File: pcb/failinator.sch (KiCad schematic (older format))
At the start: 18 parts, among them P1 CONN_01X04, P2 CONN_01X10, P3 CONN_01X10, P4 CONN_01X06, U1 MAX7219, U2 RASPIPLUSHEADER

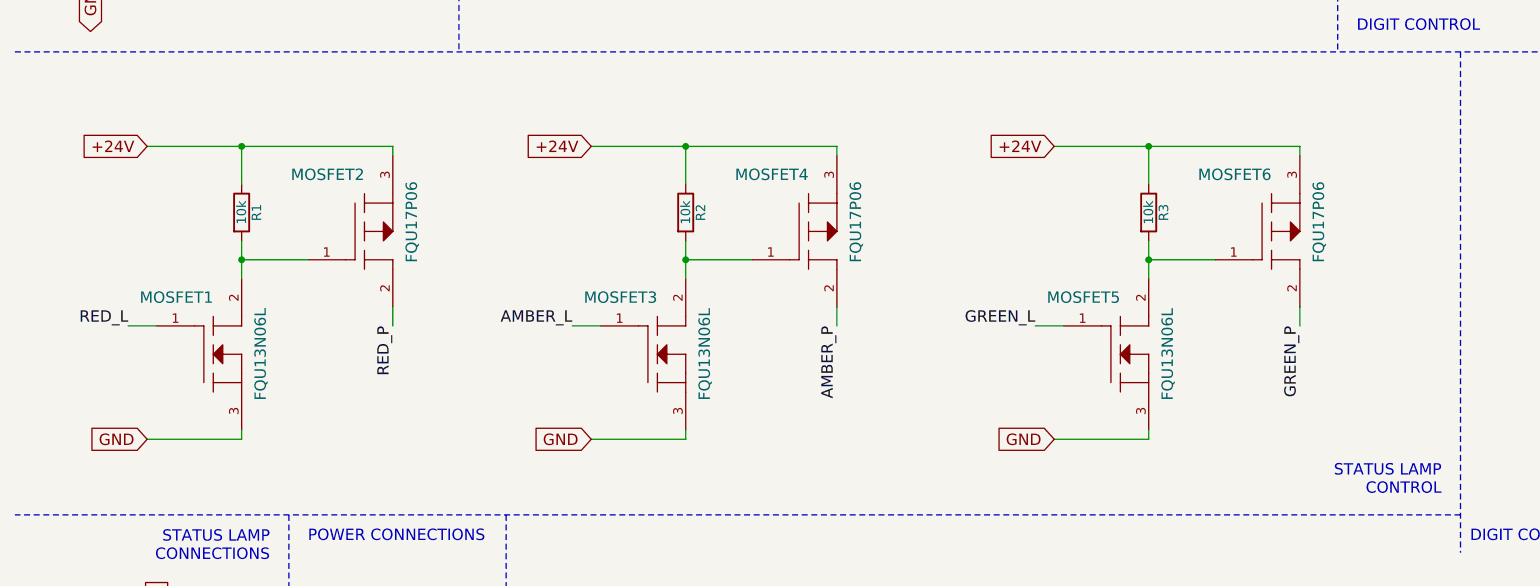
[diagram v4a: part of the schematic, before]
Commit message: Factor out the MOSFET switches into a separate sheet.
There will be a lot more of these soon once we start using a similar
pattern to switch the LED segments.
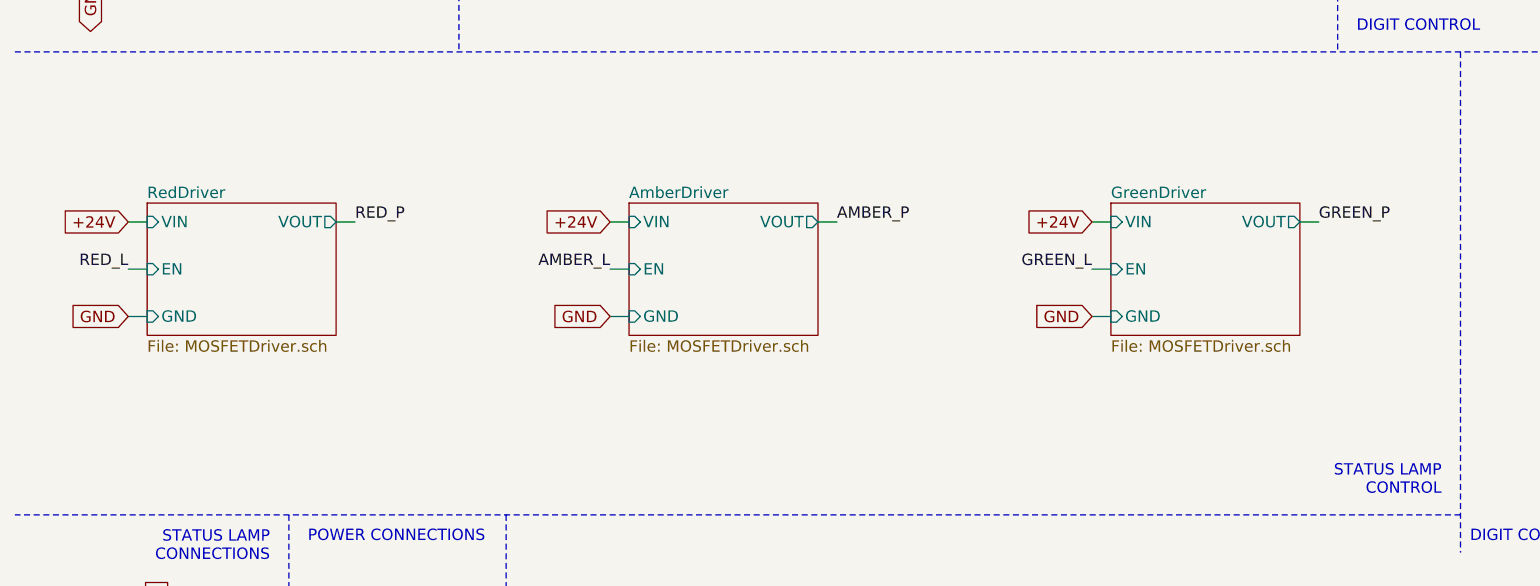
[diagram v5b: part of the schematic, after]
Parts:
- removed MOSFET1, MOSFET3, MOSFET5: FQU13N06L, failinator:TO-251AA, symbol FQU13N06L
- removed MOSFET2, MOSFET4, MOSFET6: FQU17P06, failinator:TO-251AA, symbol FQU17P06
- removed R1, R2, R3: 10k, Discret:R3, symbol R
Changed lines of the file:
@@
 $Descr USLetter 11000 8500
 encoding utf-8
-Sheet 1 1
+Sheet 1 4
 Title "Failinator"
 Date ""
@@
 Wire Wire Line
 	1350 7550 1400 7550
-$Comp
-L FQU13N06L MOSFET1
-U 1 1 5604F114
-P 1500 5700
-F 0 "MOSFET1" H 1650 6000 60  0000 R CNN
-F 1 "FQU13N06L" V 1900 5700 60  0000 C CNN
-F 2 "failinator:TO-251AA" H 1500 5700 60  0001 C CNN
-F 3 "" H 1500 5700 60  0000 C CNN
-	1    1500 5700
-	1    0    0    -1
-$EndComp
-Text GLabel 1300 6150 0    60   Input ~ 0
-GND
-Text GLabel 1300 4600 0    60   Input ~ 0
+Text GLabel 1200 5500 0    60   Input ~ 0
+GND
+Text GLabel 1200 5000 0    60   Input ~ 0
 +24V
-$Comp
-L R R1
-U 1 1 5604FF36
-P 1800 4950
-F 0 "R1" V 1880 4950 50  0000 C CNN
-F 1 "10k" V 1800 4950 50  0000 C CNN
-F 2 "Discret:R3" V 1730 4950 30  0001 C CNN
-F 3 "" H 1800 4950 30  0000 C CNN
-	1    1800 4950
-	1    0    0    -1
-$EndComp
-$Comp
-L FQU17P06 MOSFET2
-U 1 1 56050258
-P 2300 5050
-F 0 "MOSFET2" H 2450 5350 60  0000 R CNN
-F 1 "FQU17P06" V 2700 5100 60  0000 C CNN
-F 2 "failinator:TO-251AA" H 2300 5050 60  0001 C CNN
-F 3 "" H 2300 5050 60  0000 C CNN
-	1    2300 5050
-	1    0    0    -1
-$EndComp
-Text Label 1200 5550 2    60   ~ 0
+Text Label 1200 5250 2    60   ~ 0
 RED_L
-Text Label 2600 5550 3    60   ~ 0
+Text Label 2400 5000 0    60   ~ 0
 RED_P
-Wire Wire Line
-	1800 4800 1800 4600
-Wire Wire Line
-	1800 5100 1800 5300
-Wire Wire Line
-	1200 5550 1350 5550
-Wire Wire Line
-	1300 6150 1800 6150
-Wire Wire Line
-	1800 6150 1800 6100
-Wire Wire Line
-	1300 4600 2600 4600
-Wire Wire Line
-	2600 4600 2600 4650
-Connection ~ 1800 4600
-Wire Wire Line
-	2600 5450 2600 5550
-Wire Wire Line
-	2150 5200 1800 5200
-Connection ~ 1800 5200
-$Comp
-L FQU13N06L MOSFET3
-U 1 1 56051AD8
-P 3850 5700
-F 0 "MOSFET3" H 4000 6000 60  0000 R CNN
-F 1 "FQU13N06L" V 4250 5700 60  0000 C CNN
-F 2 "failinator:TO-251AA" H 3850 5700 60  0001 C CNN
-F 3 "" H 3850 5700 60  0000 C CNN
-	1    3850 5700
-	1    0    0    -1
-$EndComp
-Text GLabel 3650 6150 0    60   Input ~ 0
-GND
-Text GLabel 3650 4600 0    60   Input ~ 0
+Text GLabel 3750 5500 0    60   Input ~ 0
+GND
+Text GLabel 3750 5000 0    60   Input ~ 0
 +24V
-$Comp
-L R R2
-U 1 1 56051AE0
-P 4150 4950
-F 0 "R2" V 4230 4950 50  0000 C CNN
-F 1 "10k" V 4150 4950 50  0000 C CNN
-F 2 "Discret:R3" V 4080 4950 30  0001 C CNN
-F 3 "" H 4150 4950 30  0000 C CNN
-	1    4150 4950
-	1    0    0    -1
-$EndComp
-$Comp
-L FQU17P06 MOSFET4
-U 1 1 56051AE6
-P 4650 5050
-F 0 "MOSFET4" H 4800 5350 60  0000 R CNN
-F 1 "FQU17P06" V 5050 5100 60  0000 C CNN
-F 2 "failinator:TO-251AA" H 4650 5050 60  0001 C CNN
-F 3 "" H 4650 5050 60  0000 C CNN
-	1    4650 5050
-	1    0    0    -1
-$EndComp
-Text Label 3550 5550 2    60   ~ 0
+Text Label 3750 5250 2    60   ~ 0
 AMBER_L
-Text Label 4950 5550 3    60   ~ 0
+Text Label 4950 5000 0    60   ~ 0
 AMBER_P
-Wire Wire Line
-	4150 4800 4150 4600
-Wire Wire Line
-	4150 5100 4150 5300
-Wire Wire Line
-	3550 5550 3700 5550
-Wire Wire Line
-	3650 6150 4150 6150
-Wire Wire Line
-	4150 6150 4150 6100
-Wire Wire Line
-	3650 4600 4950 4600
-Wire Wire Line
-	4950 4600 4950 4650
-Connection ~ 4150 4600
-Wire Wire Line
-	4950 5450 4950 5550
-Wire Wire Line
-	4500 5200 4150 5200
-Connection ~ 4150 5200
-$Comp
-L FQU13N06L MOSFET5
-U 1 1 56051BEF
-P 6300 5700
-F 0 "MOSFET5" H 6450 6000 60  0000 R CNN
-F 1 "FQU13N06L" V 6700 5700 60  0000 C CNN
-F 2 "failinator:TO-251AA" H 6300 5700 60  0001 C CNN
-F 3 "" H 6300 5700 60  0000 C CNN
-	1    6300 5700
-	1    0    0    -1
-$EndComp
-Text GLabel 6100 6150 0    60   Input ~ 0
-GND
-Text GLabel 6100 4600 0    60   Input ~ 0
+Text GLabel 6300 5500 0    60   Input ~ 0
+GND
+Text GLabel 6300 5000 0    60   Input ~ 0
 +24V
-$Comp
-L R R3
-U 1 1 56051BF7
-P 6600 4950
-F 0 "R3" V 6680 4950 50  0000 C CNN
-F 1 "10k" V 6600 4950 50  0000 C CNN
-F 2 "Discret:R3" V 6530 4950 30  0001 C CNN
-F 3 "" H 6600 4950 30  0000 C CNN
-	1    6600 4950
-	1    0    0    -1
-$EndComp
-$Comp
-L FQU17P06 MOSFET6
-U 1 1 56051BFD
-P 7100 5050
-F 0 "MOSFET6" H 7250 5350 60  0000 R CNN
-F 1 "FQU17P06" V 7500 5100 60  0000 C CNN
-F 2 "failinator:TO-251AA" H 7100 5050 60  0001 C CNN
-F 3 "" H 7100 5050 60  0000 C CNN
-	1    7100 5050
-	1    0    0    -1
-$EndComp
-Text Label 6000 5550 2    60   ~ 0
+Text Label 6300 5250 2    60   ~ 0
 GREEN_L
-Text Label 7400 5550 3    60   ~ 0
+Text Label 7500 5000 0    60   ~ 0
 GREEN_P
-Wire Wire Line
-	6600 4800 6600 4600
-Wire Wire Line
-	6600 5100 6600 5300
-Wire Wire Line
-	6000 5550 6150 5550
-Wire Wire Line
-	6100 6150 6600 6150
-Wire Wire Line
-	6600 6150 6600 6100
-Wire Wire Line
-	6100 4600 7400 4600
-Wire Wire Line
-	7400 4600 7400 4650
-Connection ~ 6600 4600
-Wire Wire Line
-	7400 5450 7400 5550
-Wire Wire Line
-	6950 5200 6600 5200
-Connection ~ 6600 5200
 Wire Notes Line
 	2950 600  2950 4100
@@
 Text Label 9250 5950 2    60   ~ 0
 DIG1
+$Sheet
+S 1300 4900 1000 700
+U 568778A1
+F0 "RedDriver" 60
+F1 "MOSFETDriver.sch" 60
+F2 "VIN" I L 1300 5000 60
+F3 "GND" I L 1300 5500 60
+F4 "EN" I L 1300 5250 60
+F5 "VOUT" O R 2300 5000 60
+$EndSheet
+Wire Wire Line
+	2300 5000 2400 5000
+Wire Wire Line
+	1200 5000 1300 5000
+Wire Wire Line
+	1200 5250 1300 5250
+Wire Wire Line
+	1200 5500 1300 5500
+$Sheet
+S 3850 4900 1000 700
+U 56879543
+F0 "AmberDriver" 60
+F1 "MOSFETDriver.sch" 60
+F2 "VIN" I L 3850 5000 60
+F3 "GND" I L 3850 5500 60
+F4 "EN" I L 3850 5250 60
+F5 "VOUT" O R 4850 5000 60
+$EndSheet
+$Sheet
+S 6400 4900 1000 700
+U 5687AB7C
+F0 "GreenDriver" 60
+F1 "MOSFETDriver.sch" 60
+F2 "VIN" I L 6400 5000 60
+F3 "GND" I L 6400 5500 60
+F4 "EN" I L 6400 5250 60
+F5 "VOUT" O R 7400 5000 60
+$EndSheet
+Wire Wire Line
+	3750 5000 3850 5000
+Wire Wire Line
+	3750 5250 3850 5250
+Wire Wire Line
+	3750 5500 3850 5500
+Wire Wire Line
+	4850 5000 4950 5000
+Wire Wire Line
+	6300 5000 6400 5000
+Wire Wire Line
+	6300 5250 6400 5250
+Wire Wire Line
+	6300 5500 6400 5500
+Wire Wire Line
+	7400 5000 7500 5000
 $EndSCHEMATC

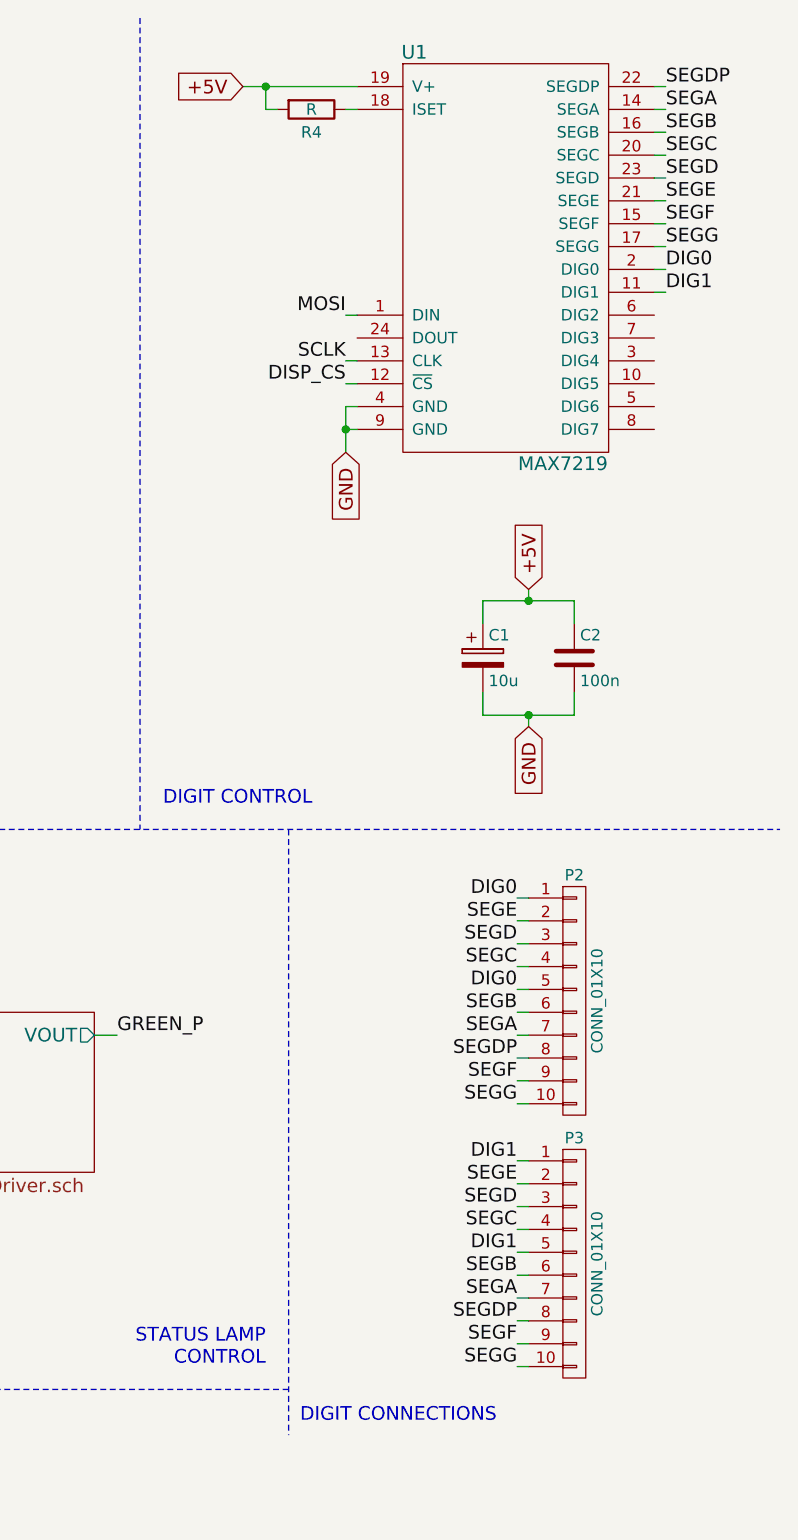
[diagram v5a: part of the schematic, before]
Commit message: Remove the MAX7219-based digit driver sub-circuit
The digit driver on v0.1 was not correct, providing only 5V to LED
segments that have a forward voltage of more like 27V, causing them to
not show at all.

A replacement for this will be added in a subsequent commit.
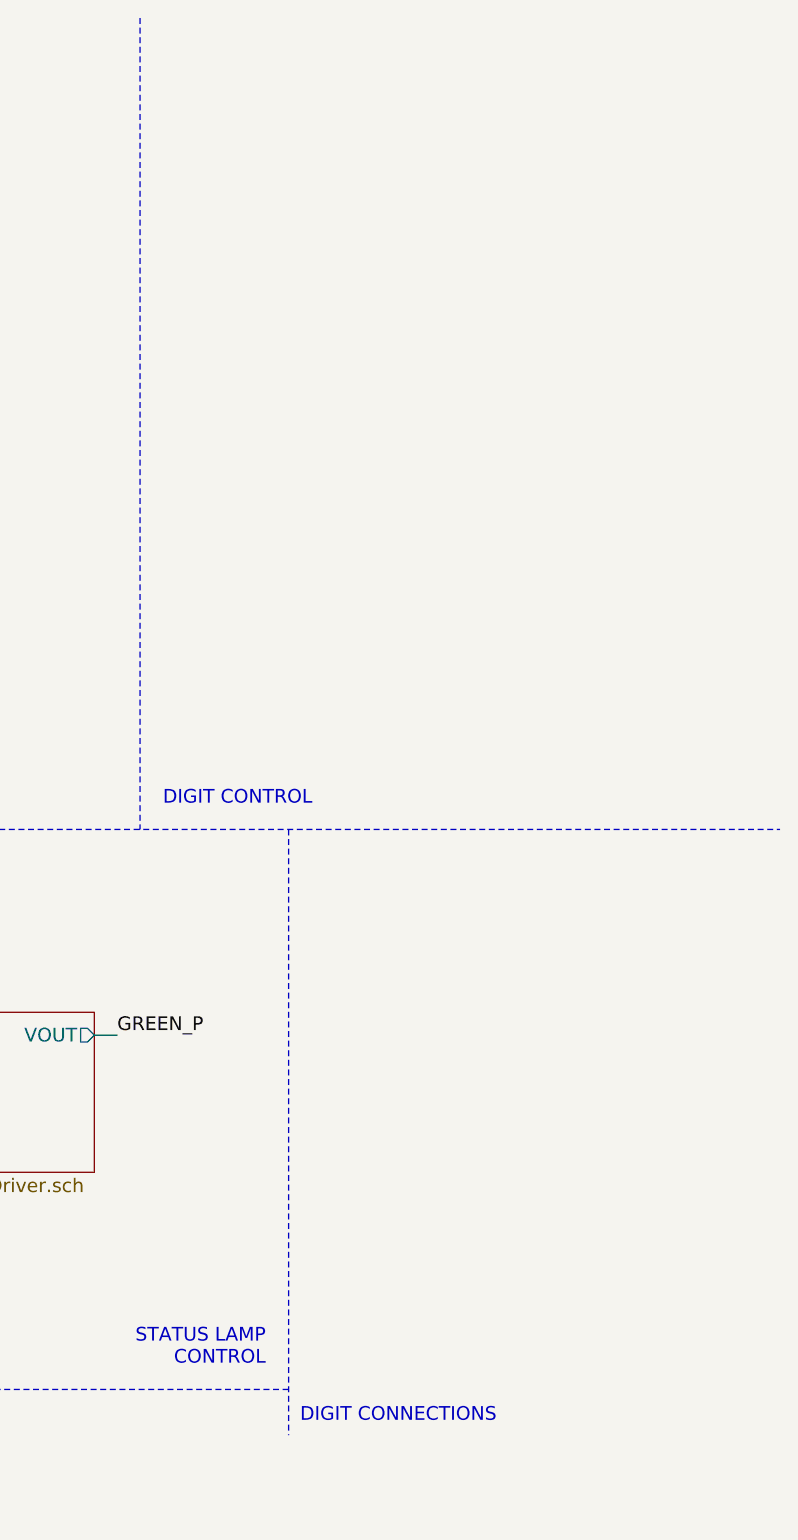
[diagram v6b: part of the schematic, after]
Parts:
- removed C1: 10u, failinator:CPOL_2mm, symbol CP
- removed C2: 100n, failinator:C_4mm, symbol C
- removed P2, P3: CONN_01X10, Pin_Headers:Pin_Header_Straight_1x10, symbol CONN_01X10
- removed R4: R, Discret:R3, symbol R
- removed U1: MAX7219, Housings_DIP:DIP-24_W7.62mm_LongPads, symbol MAX7219
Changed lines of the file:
@@
 Wire Wire Line
 	2350 3400 2400 3400
-$Comp
-L MAX7219 U1
-U 1 1 5604CE76
-P 9200 1600
-F 0 "U1" H 8800 2500 60  0000 C CNN
-F 1 "MAX7219" H 9450 700 60  0000 C CNN
-F 2 "Housings_DIP:DIP-24_W7.62mm_LongPads" H 9050 2100 60  0001 C CNN
-F 3 "" H 9050 2100 60  0000 C CNN
-	1    9200 1600
-	1    0    0    -1
-$EndComp
-Text GLabel 8050 850  0    60   Input ~ 0
-+5V
-$Comp
-L R R4
-U 1 1 5604CF10
-P 8350 950
-F 0 "R4" V 8450 950 50  0000 C CNN
-F 1 "R" V 8350 950 50  0000 C CNN
-F 2 "Discret:R3" V 8280 950 30  0001 C CNN
-F 3 "" H 8350 950 30  0000 C CNN
-	1    8350 950
-	0    1    1    0
-$EndComp
-Wire Wire Line
-	8500 950  8550 950
-Wire Wire Line
-	8050 850  8550 850
-Wire Wire Line
-	8200 950  8150 950
-Wire Wire Line
-	8150 950  8150 850
-Connection ~ 8150 850
-Text GLabel 8500 2450 3    60   Input ~ 0
-GND
-Wire Wire Line
-	8500 2450 8500 2250
-Wire Wire Line
-	8500 2250 8550 2250
-Wire Wire Line
-	8500 2350 8550 2350
-Connection ~ 8500 2350
-Text Label 8500 1850 2    60   ~ 0
-MOSI
-Text Label 8500 2050 2    60   ~ 0
-SCLK
-Text Label 8500 2150 2    60   ~ 0
-DISP_CS
-Wire Wire Line
-	8500 2150 8550 2150
-Wire Wire Line
-	8500 2050 8550 2050
-Wire Wire Line
-	8500 1850 8550 1850
-$Comp
-L CONN_01X10 P2
-U 1 1 5604D28A
-P 9500 4850
-F 0 "P2" H 9500 5400 50  0000 C CNN
-F 1 "CONN_01X10" V 9600 4850 50  0000 C CNN
-F 2 "Pin_Headers:Pin_Header_Straight_1x10" H 9500 4850 60  0001 C CNN
-F 3 "" H 9500 4850 60  0000 C CNN
-	1    9500 4850
-	1    0    0    -1
-$EndComp
-$Comp
-L CONN_01X10 P3
-U 1 1 5604D2BB
-P 9500 6000
-F 0 "P3" H 9500 6550 50  0000 C CNN
-F 1 "CONN_01X10" V 9600 6000 50  0000 C CNN
-F 2 "Pin_Headers:Pin_Header_Straight_1x10" H 9500 6000 60  0001 C CNN
-F 3 "" H 9500 6000 60  0000 C CNN
-	1    9500 6000
-	1    0    0    -1
-$EndComp
-Text Label 9900 850  0    60   ~ 0
-SEGDP
-Text Label 9900 950  0    60   ~ 0
-SEGA
-Text Label 9900 1050 0    60   ~ 0
-SEGB
-Text Label 9900 1150 0    60   ~ 0
-SEGC
-Text Label 9900 1250 0    60   ~ 0
-SEGD
-Text Label 9900 1350 0    60   ~ 0
-SEGE
-Text Label 9900 1450 0    60   ~ 0
-SEGF
-Text Label 9900 1550 0    60   ~ 0
-SEGG
-Text Label 9900 1650 0    60   ~ 0
-DIG0
-Text Label 9900 1750 0    60   ~ 0
-DIG1
-Wire Wire Line
-	9850 850  9900 850
-Wire Wire Line
-	9850 950  9900 950
-Wire Wire Line
-	9850 1050 9900 1050
-Wire Wire Line
-	9850 1150 9900 1150
-Wire Wire Line
-	9850 1250 9900 1250
-Wire Wire Line
-	9850 1350 9900 1350
-Wire Wire Line
-	9850 1450 9900 1450
-Wire Wire Line
-	9850 1550 9900 1550
-Wire Wire Line
-	9850 1650 9900 1650
-Wire Wire Line
-	9850 1750 9900 1750
-Text Label 9250 4400 2    60   ~ 0
-DIG0
-Text Label 9250 5550 2    60   ~ 0
-DIG1
-Wire Wire Line
-	9250 5100 9300 5100
-Wire Wire Line
-	9250 6250 9300 6250
-Text Label 9250 5650 2    60   ~ 0
-SEGE
-Text Label 9250 4500 2    60   ~ 0
-SEGE
-Text Label 9250 4600 2    60   ~ 0
-SEGD
-Text Label 9250 5750 2    60   ~ 0
-SEGD
-Text Label 9250 5100 2    60   ~ 0
-SEGDP
-Text Label 9250 6250 2    60   ~ 0
-SEGDP
-Text Label 9250 4700 2    60   ~ 0
-SEGC
-Text Label 9250 4900 2    60   ~ 0
-SEGB
-Text Label 9250 5000 2    60   ~ 0
-SEGA
-Text Label 9250 5850 2    60   ~ 0
-SEGC
-Text Label 9250 6050 2    60   ~ 0
-SEGB
-Text Label 9250 6150 2    60   ~ 0
-SEGA
-Text Label 9250 5300 2    60   ~ 0
-SEGG
-Text Label 9250 5200 2    60   ~ 0
-SEGF
-Text Label 9250 6450 2    60   ~ 0
-SEGG
-Text Label 9250 6350 2    60   ~ 0
-SEGF
-Wire Wire Line
-	9250 4400 9300 4400
-Wire Wire Line
-	9250 4500 9300 4500
-Wire Wire Line
-	9250 4700 9300 4700
-Wire Wire Line
-	9250 4800 9300 4800
-Wire Wire Line
-	9250 4900 9300 4900
-Wire Wire Line
-	9250 5000 9300 5000
-Wire Wire Line
-	9250 5200 9300 5200
-Wire Wire Line
-	9250 5300 9300 5300
-Wire Wire Line
-	9250 5550 9300 5550
-Wire Wire Line
-	9250 5650 9300 5650
-Wire Wire Line
-	9250 5850 9300 5850
-Wire Wire Line
-	9250 5950 9300 5950
-Wire Wire Line
-	9250 6050 9300 6050
-Wire Wire Line
-	9250 6150 9300 6150
-Wire Wire Line
-	9250 6350 9300 6350
-Wire Wire Line
-	9250 6450 9300 6450
-$Comp
-L CP C1
-U 1 1 5604DF59
-P 9100 3350
-F 0 "C1" H 9125 3450 50  0000 L CNN
-F 1 "10u" H 9125 3250 50  0000 L CNN
-F 2 "failinator:CPOL_2mm" H 9138 3200 30  0001 C CNN
-F 3 "" H 9100 3350 60  0000 C CNN
-	1    9100 3350
-	1    0    0    -1
-$EndComp
-$Comp
-L C C2
-U 1 1 5604DF92
-P 9500 3350
-F 0 "C2" H 9525 3450 50  0000 L CNN
-F 1 "100n" H 9525 3250 50  0000 L CNN
-F 2 "failinator:C_4mm" H 9538 3200 30  0001 C CNN
-F 3 "" H 9500 3350 60  0000 C CNN
-	1    9500 3350
-	1    0    0    -1
-$EndComp
-Text GLabel 9300 3050 1    60   Input ~ 0
-+5V
-Text GLabel 9300 3650 3    60   Input ~ 0
-GND
-Wire Wire Line
-	9300 3050 9300 3100
-Wire Wire Line
-	9100 3100 9100 3200
-Connection ~ 9300 3100
-Wire Wire Line
-	9100 3100 9500 3100
-Wire Wire Line
-	9500 3100 9500 3200
-Wire Wire Line
-	9100 3500 9100 3600
-Wire Wire Line
-	9100 3600 9500 3600
-Wire Wire Line
-	9300 3600 9300 3650
-Wire Wire Line
-	9500 3600 9500 3500
-Connection ~ 9300 3600
 Text Label 2400 1100 0    60   ~ 0
 RED_L
@@
 Text Notes 2150 6700 0    60   ~ 0
 POWER CONNECTIONS
-Wire Wire Line
-	9250 4600 9300 4600
-Text Label 9250 4800 2    60   ~ 0
-DIG0
-Wire Wire Line
-	9250 5750 9300 5750
-Text Label 9250 5950 2    60   ~ 0
-DIG1
 $Sheet
 S 1300 4900 1000 700
